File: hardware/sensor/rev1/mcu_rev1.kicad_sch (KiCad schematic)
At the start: 14 parts, among them IC1 STM8L051F3P6, J1 22-28-4044, J2 M20-9770342

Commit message: EG-49 All components reviewed, MCU and RF.
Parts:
- renumbered C3 to C2, C4 to C3, C5 to C4
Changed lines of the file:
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@@
 		(dnp no)
 		(fields_autoplaced yes)
-		(property "Reference" "C5"
+		(property "Reference" "C4"
 			(at 43.18 162.5599 0)
 			(effects
@@
 			(project "sensor_rev1"
 				(path "/d3cb7130-decc-418b-958e-e5d84a8d867f/ec220677-d66d-4ee1-961f-1c93fb46783a"
-					(reference "C5")
+					(reference "C4")
 					(unit 1)
 				)
@@
 		(dnp no)
 		(fields_autoplaced yes)
-		(property "Reference" "C3"
+		(property "Reference" "C2"
 			(at 191.77 77.4699 0)
 			(effects
@@
 			(project "sensor_rev1"
 				(path "/d3cb7130-decc-418b-958e-e5d84a8d867f/ec220677-d66d-4ee1-961f-1c93fb46783a"
-					(reference "C3")
+					(reference "C2")
 					(unit 1)
 				)
@@
 		(dnp no)
 		(fields_autoplaced yes)
-		(property "Reference" "C4"
+		(property "Reference" "C3"
 			(at 66.04 125.7299 0)
 			(effects
@@
 			(project "sensor_rev1"
 				(path "/d3cb7130-decc-418b-958e-e5d84a8d867f/ec220677-d66d-4ee1-961f-1c93fb46783a"
-					(reference "C4")
-					(unit 1)
-				)
+					(reference "C3")
+					(unit 1)
+				)

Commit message: EG-49 All  components parameters standardized for mouser.
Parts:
- C2: Manufacturer KEMET -> (none); Manufacturer Part Number C0603C102K8RACTU -> (none); Manufacturer_Name (none) -> KEMET; Manufacturer_Part_Number (none) -> C0603C102K8RACTU; Mouser Price/Stock (none) -> https://www.mouser.co.uk/en/ProductDetail/KEMET/C0603C102K8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; Supplier Link https://www.mouser.co.uk/en/ProductDetail/KEMET/C0603C102K8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 -> (none)
- C3: Manufacturer Wurth Elektronik -> (none); Manufacturer Part Number 885012206020 -> (none); Manufacturer_Name (none) -> Wurth Elektronik; Manufacturer_Part_Number (none) -> 885012206020; Mouser Price/Stock (none) -> https://pt.mouser.com/en/ProductDetail/Wurth-Elektronik/885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; Supplier Link https://pt.mouser.com/en/ProductDetail/Wurth-Elektronik/885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 -> (none)
- C4: Manufacturer YAGEO -> (none); Manufacturer Part Number CC0603KRX7R6BB103 -> (none); Manufacturer_Name (none) -> YAGEO; Manufacturer_Part_Number (none) -> CC0603KRX7R6BB103; Mouser Price/Stock (none) -> https://pt.mouser.com/en/ProductDetail/YAGEO/CC0603KRX7R6BB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; Supplier Link https://pt.mouser.com/en/ProductDetail/YAGEO/CC0603KRX7R6BB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 -> (none)
- J2: Manufacturer Harwin -> (none); Manufacturer Part Number M20-9770342 -> (none); Manufacturer_Name (none) -> Harwin; Manufacturer_Part_Number (none) -> M20-9770342; Mouser Price/Stock (none) -> https://www.mouser.co.uk/ProductDetail/Harwin/M20-9770342?q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; Supplier Link https://www.mouser.co.uk/ProductDetail/Harwin/M20-9770342?q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 -> (none)
- R1: Manufacturer Yageo -> (none); Manufacturer Part Number RC0603JR-13100RL -> (none); Manufacturer_Name (none) -> Yageo; Manufacturer_Part_Number (none) -> RC0603JR-13100RL; Mouser Price/Stock (none) -> https://pt.mouser.com/en/ProductDetail/YAGEO/RC0603JR-13100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; Supplier Link https://pt.mouser.com/en/ProductDetail/YAGEO/RC0603JR-13100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 -> (none)
- R2: Manufacturer Yageo -> (none); Manufacturer Part Number AA0603FR-072M2L -> (none); Manufacturer_Name (none) -> Yageo; Manufacturer_Part_Number (none) -> AA0603FR-072M2L; Mouser Price/Stock (none) -> https://pt.mouser.com/en/ProductDetail/YAGEO/AA0603FR-072M2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; Supplier Link https://pt.mouser.com/en/ProductDetail/YAGEO/AA0603FR-072M2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 -> (none)
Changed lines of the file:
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@@
 			)
 		)
-		(property "Supplier Link" "https://www.mouser.co.uk/ProductDetail/Harwin/M20-9770342?qs=Jph8NoUxIfVskiTzAX%252BIFA%3D%3D"
+		(property "Mouser Price/Stock" "https://www.mouser.co.uk/ProductDetail/Harwin/M20-9770342?qs=Jph8NoUxIfVskiTzAX%252BIFA%3D%3D"
 			(at 176.53 620.32 0)
 			(effects
@@
 			)
 		)
-		(property "Manufacturer" "Harwin"
+		(property "Manufacturer_Name" "Harwin"
 			(at 176.53 720.32 0)
 			(effects
@@
 			)
 		)
-		(property "Manufacturer Part Number" "M20-9770342"
+		(property "Manufacturer_Part_Number" "M20-9770342"
 			(at 176.53 820.32 0)
 			(effects
@@
 			)
 		)
-		(property "Supplier Link" "https://pt.mouser.com/en/ProductDetail/YAGEO/RC0603JR-13100RL?qs=sGAEpiMZZMvdGkrng054t8AJgcdMkx7xkQkRKZbeqEI%3D"
+		(property "Mouser Price/Stock" "https://pt.mouser.com/en/ProductDetail/YAGEO/RC0603JR-13100RL?qs=sGAEpiMZZMvdGkrng054t8AJgcdMkx7xkQkRKZbeqEI%3D"
 			(at 35.56 78.74 0)
 			(effects
@@
 			)
 		)
-		(property "Manufacturer" "Yageo"
+		(property "Manufacturer_Name" "Yageo"
 			(at 35.56 78.74 0)
 			(effects
@@
 			)
 		)
-		(property "Manufacturer Part Number" "RC0603JR-13100RL "
+		(property "Manufacturer_Part_Number" "RC0603JR-13100RL "
 			(at 35.56 78.74 0)
 			(effects
@@
 			)
 		)
-		(property "Supplier Link" "https://pt.mouser.com/en/ProductDetail/YAGEO/CC0603KRX7R6BB103?qs=sGAEpiMZZMvsSlwiRhF8qtVFUj6yLw9vFdzWWJmGTI0%3D"
+		(property "Mouser Price/Stock" "https://pt.mouser.com/en/ProductDetail/YAGEO/CC0603KRX7R6BB103?qs=sGAEpiMZZMvsSlwiRhF8qtVFUj6yLw9vFdzWWJmGTI0%3D"
 			(at 39.37 163.83 0)
 			(effects
@@
 			)
 		)
-		(property "Manufacturer" "YAGEO"
+		(property "Manufacturer_Name" "YAGEO"
 			(at 39.37 163.83 0)
 			(effects
@@
 			)
 		)
-		(property "Manufacturer Part Number" "CC0603KRX7R6BB103"
+		(property "Manufacturer_Part_Number" "CC0603KRX7R6BB103"
 			(at 39.37 163.83 0)
 			(effects
@@
 			)
 		)
-		(property "Supplier Link" "https://pt.mouser.com/en/ProductDetail/YAGEO/AA0603FR-072M2L?qs=sGAEpiMZZMvdGkrng054txzUp8gpcBx9hhxvQIhjhzKzivkvqefGPg%3D%3D"
+		(property "Mouser Price/Stock" "https://pt.mouser.com/en/ProductDetail/YAGEO/AA0603FR-072M2L?qs=sGAEpiMZZMvdGkrng054txzUp8gpcBx9hhxvQIhjhzKzivkvqefGPg%3D%3D"
 			(at 172.72 62.23 0)
 			(effects
@@
 			)
 		)
-		(property "Manufacturer" "Yageo"
+		(property "Manufacturer_Name" "Yageo"
 			(at 172.72 62.23 0)
 			(effects
@@
 			)
 		)
-		(property "Manufacturer Part Number" "AA0603FR-072M2L"
+		(property "Manufacturer_Part_Number" "AA0603FR-072M2L"
 			(at 172.72 62.23 0)
 			(effects
@@
 			)
 		)
-		(property "Supplier Link" "https://www.mouser.co.uk/en/ProductDetail/KEMET/C0603C102K8RACTU?qs=sGAEpiMZZMvsSlwiRhF8quIsB1QHp5lfG10MayaV%252Bl0%3D"
+		(property "Mouser Price/Stock" "https://www.mouser.co.uk/en/ProductDetail/KEMET/C0603C102K8RACTU?qs=sGAEpiMZZMvsSlwiRhF8quIsB1QHp5lfG10MayaV%252Bl0%3D"
 			(at 187.96 78.74 0)
 			(effects
@@
 			)
 		)
-		(property "Manufacturer" "KEMET"
+		(property "Manufacturer_Name" "KEMET"
 			(at 187.96 78.74 0)
 			(effects
@@
 			)
 		)
-		(property "Manufacturer Part Number" "C0603C102K8RACTU "
+		(property "Manufacturer_Part_Number" "C0603C102K8RACTU "
 			(at 187.96 78.74 0)
 			(effects
@@
 			)
 		)
-		(property "Supplier Link" "https://pt.mouser.com/en/ProductDetail/Wurth-Elektronik/885012206020?qs=sGAEpiMZZMvsSlwiRhF8qunkWFWGyo%252Bv87eLmDBMvaFF4rJhETyCbg%3D%3D"
+		(property "Mouser Price/Stock" "https://pt.mouser.com/en/ProductDetail/Wurth-Elektronik/885012206020?qs=sGAEpiMZZMvsSlwiRhF8qunkWFWGyo%252Bv87eLmDBMvaFF4rJhETyCbg%3D%3D"
 			(at 62.23 127 0)
 			(effects
@@
 			)
 		)
-		(property "Manufacturer" "Wurth Elektronik"
+		(property "Manufacturer_Name" "Wurth Elektronik"
 			(at 62.23 127 0)
 			(effects
@@
 			)
 		)
-		(property "Manufacturer Part Number" "885012206020"
+		(property "Manufacturer_Part_Number" "885012206020"
 			(at 62.23 127 0)
 			(effects

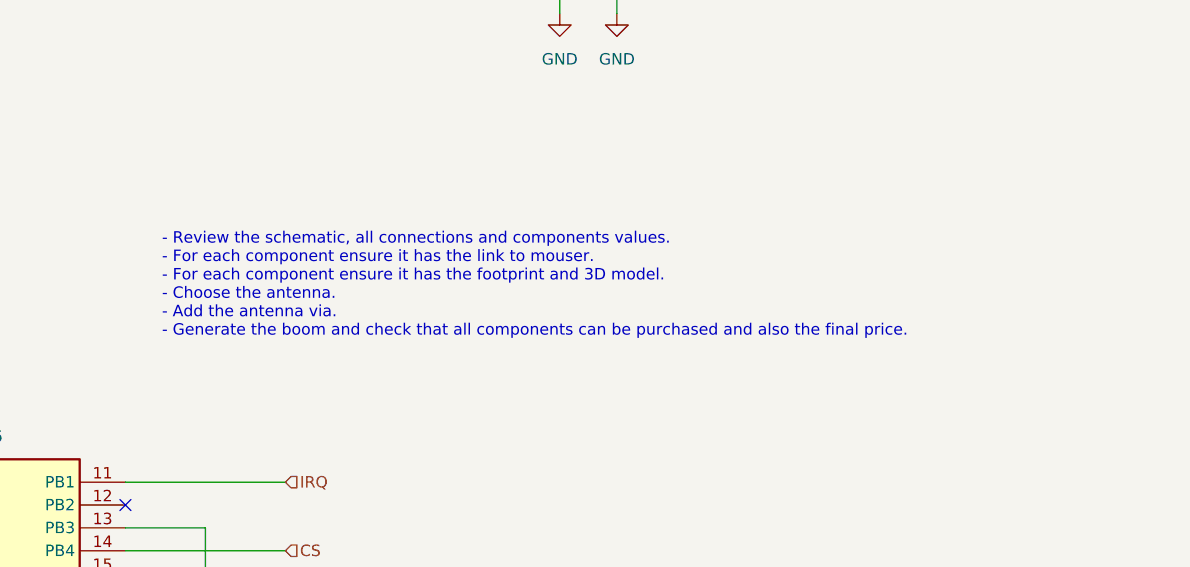
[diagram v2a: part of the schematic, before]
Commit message: EG-49 Antenna hole placed.
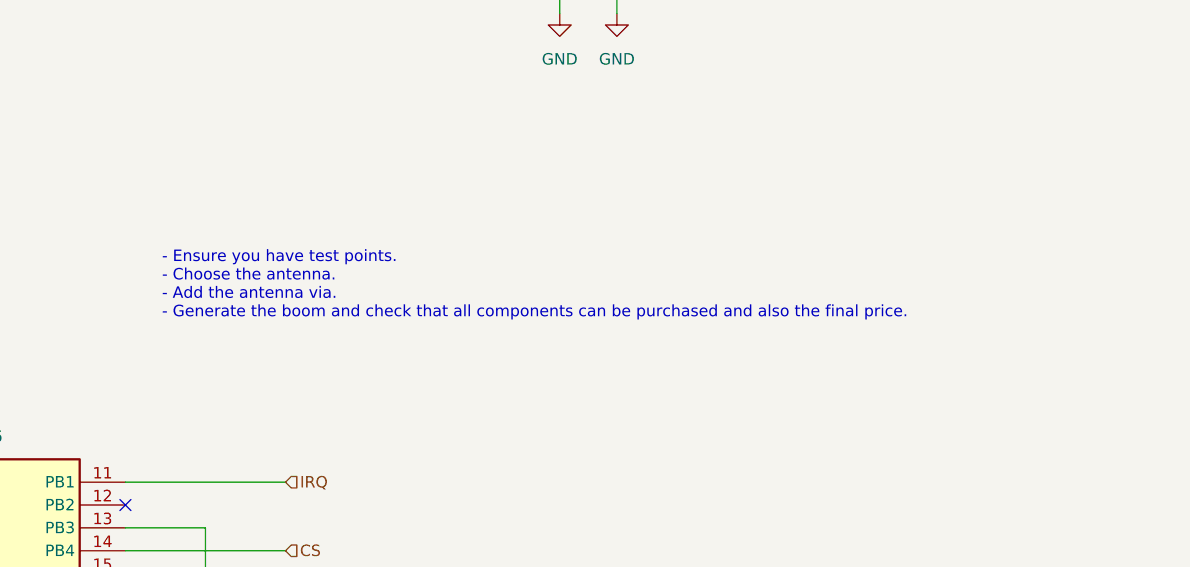
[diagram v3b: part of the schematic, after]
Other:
- note added: "- Ensure you have test points. - Choose the antenna. - Add the antenna via. - Generate the boom and check that all components can be purchased and also the final price."
- note removed: "- Review the schematic, all connections and components values. - For each component ensure it has the link to mouser. - For each component ensure it has the footprint and 3D model. - Choose the antenna. - Add the antenna via. - Generate the boom and check that all components can be purchased and also the final price."
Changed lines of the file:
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@@
 		)
 	)
-	(text "- Review the schematic, all connections and components values.\n- For each component ensure it has the link to mouser.\n- For each component ensure it has the footprint and 3D model.\n- Choose the antenna.\n- Add the antenna via.\n- Generate the boom and check that all components can be purchased and also the final price."
+	(text "- Ensure you have test points.\n- Choose the antenna.\n- Add the antenna via.\n- Generate the boom and check that all components can be purchased and also the final price."
 		(exclude_from_sim no)
 		(at 128.524 126.746 0)

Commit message: EG-49 Adjust antenna place in PCB.
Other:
- note added: "- Ensure you have test points. - Check all MCU pins once again. - Check the pull-ups enabled by SW in STM8 HAL library. - Generate the boom and check that all components can be purchased and also the final price. - Ensure ERC errros and warnings are 0."
- note removed: "- Ensure you have test points. - Choose the antenna. - Add the antenna via. - Generate the boom and check that all components can be purchased and also the final price."
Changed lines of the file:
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@@
 		)
 	)
-	(text "- Ensure you have test points.\n- Choose the antenna.\n- Add the antenna via.\n- Generate the boom and check that all components can be purchased and also the final price."
+	(text "- Ensure you have test points.\n- Check all MCU pins once again.\n- Check the pull-ups enabled by SW in STM8 HAL library.\n- Generate the boom and check that all components can be purchased and also the final price.\n- Ensure ERC errros and warnings are 0."
 		(exclude_from_sim no)
 		(at 128.524 126.746 0)

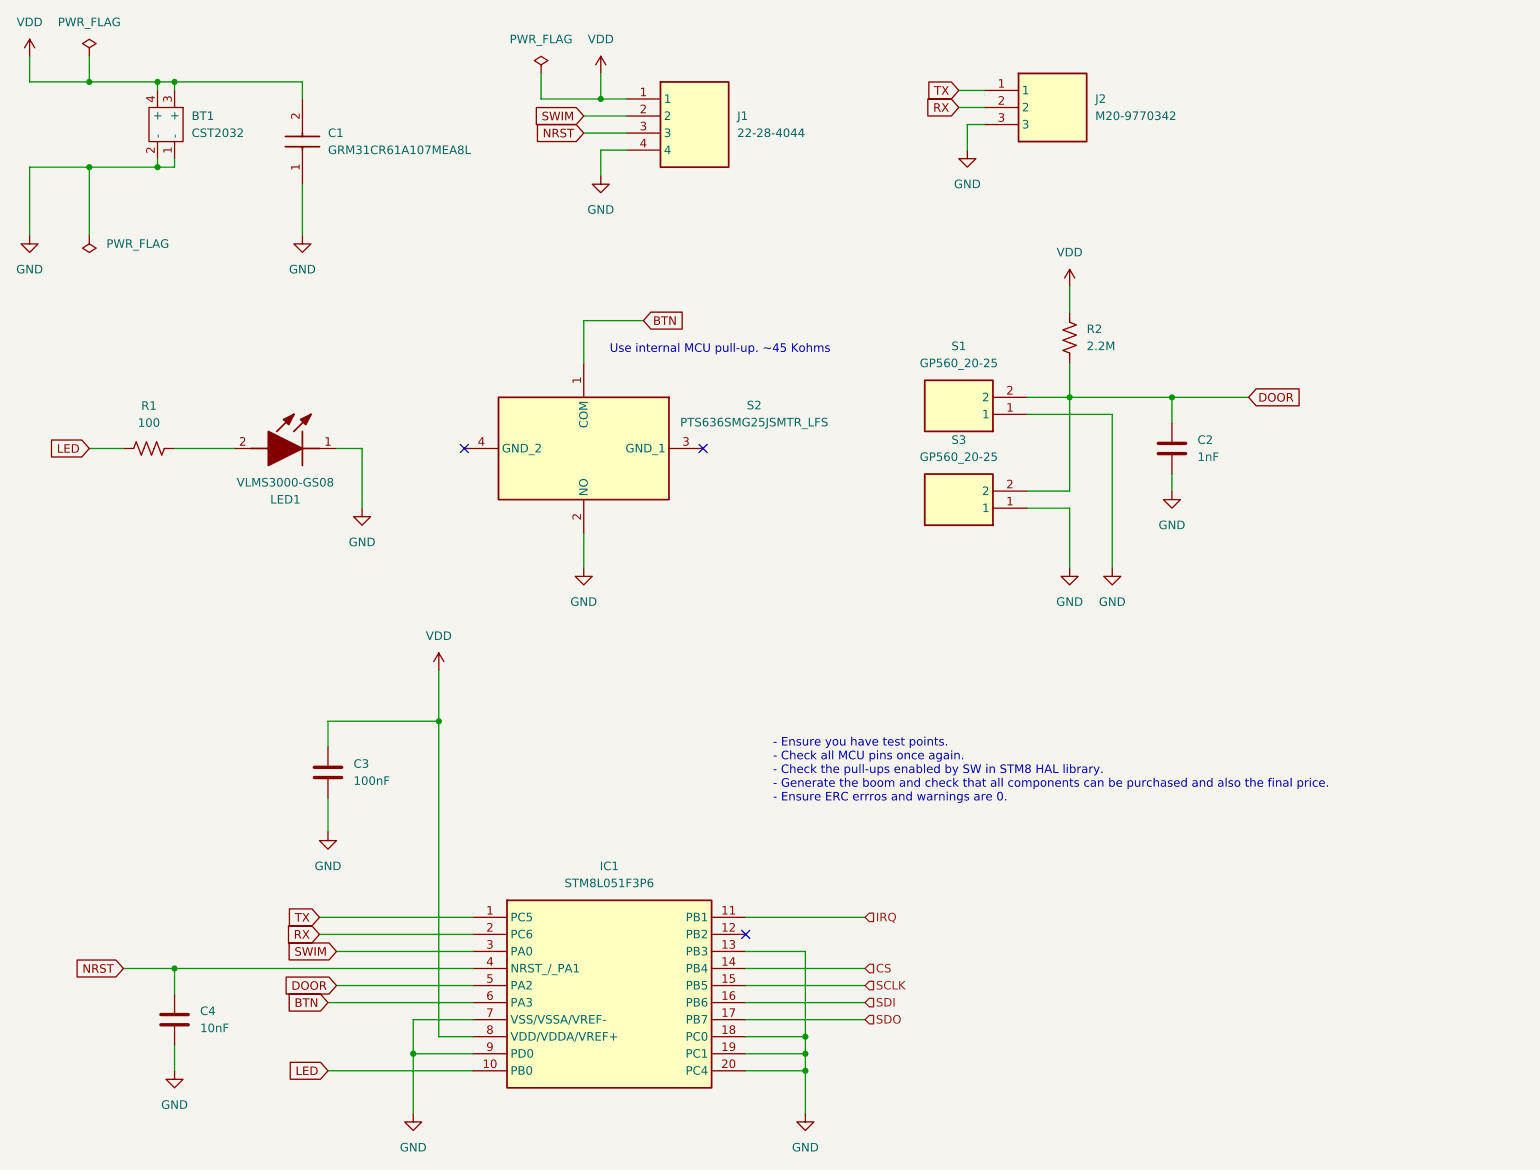
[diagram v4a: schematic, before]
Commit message: EG-49 Tests points added.
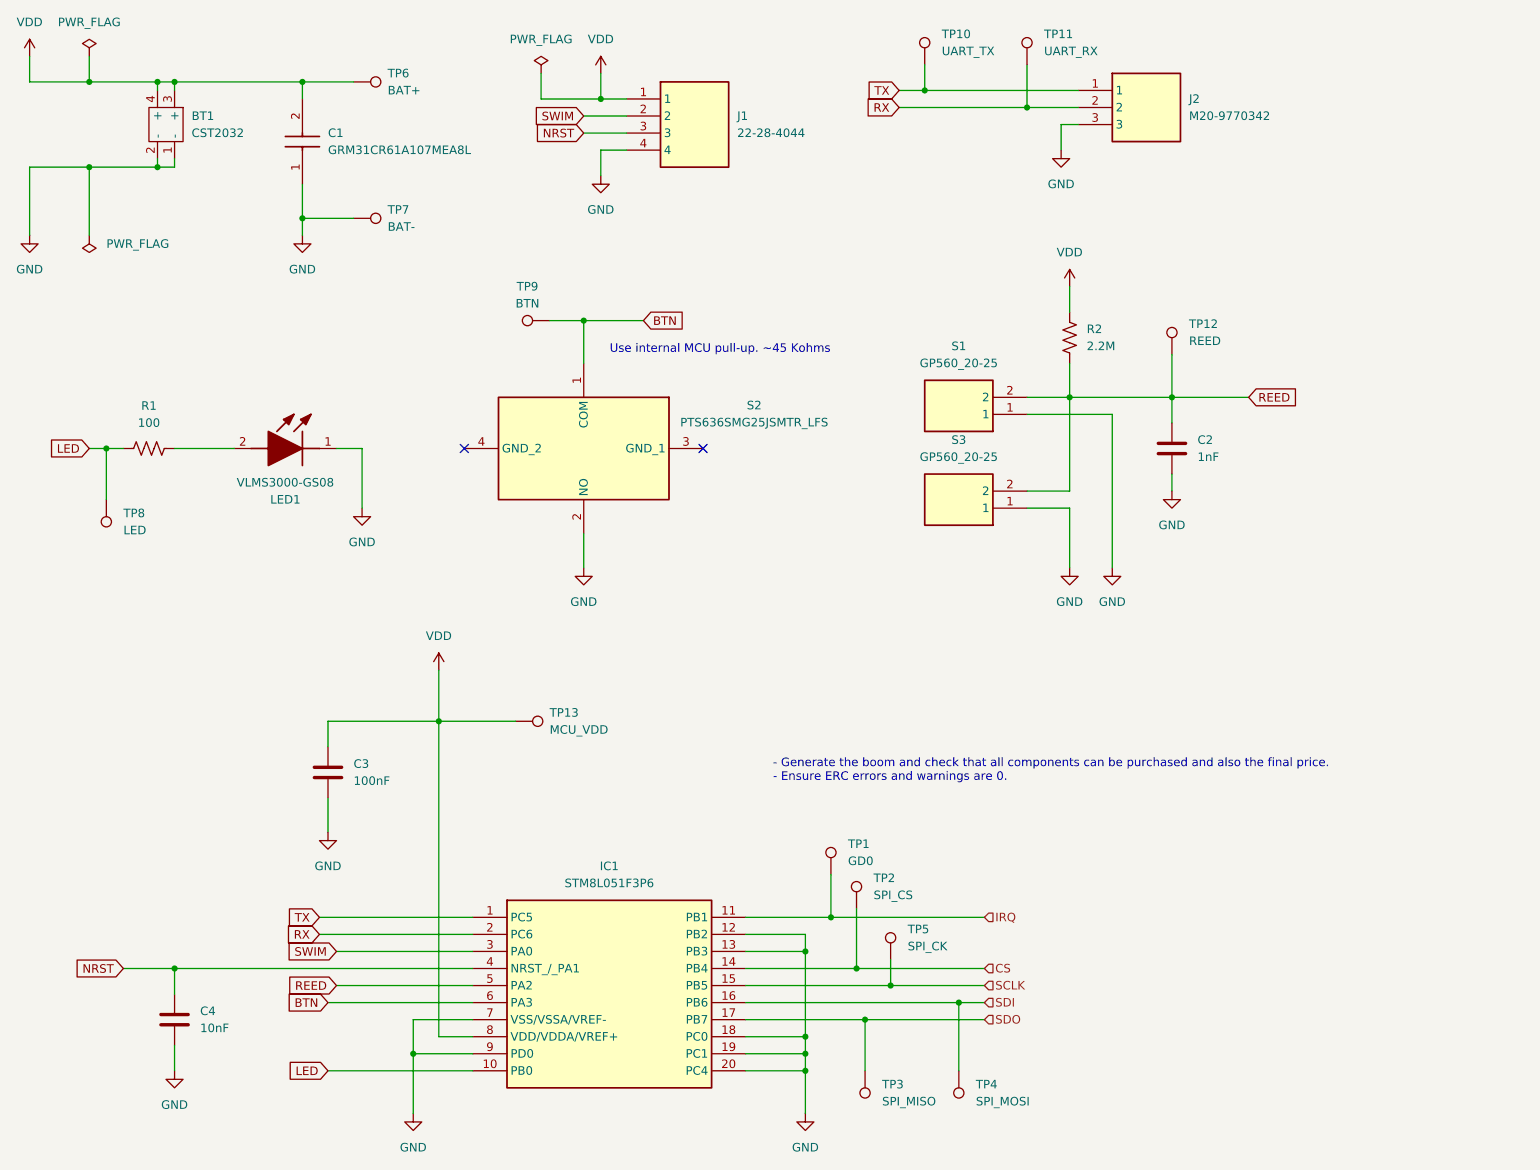
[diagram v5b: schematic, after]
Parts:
- added TP1: GD0, TestPoint:TestPoint_Pad_D1.0mm, symbol Connector:TestPoint
- added TP10: UART_TX, TestPoint:TestPoint_Pad_D1.0mm, symbol Connector:TestPoint
- added TP11: UART_RX, TestPoint:TestPoint_Pad_D1.0mm, symbol Connector:TestPoint
- added TP12: REED, TestPoint:TestPoint_Pad_D1.0mm, symbol Connector:TestPoint
- added TP13: MCU_VDD, TestPoint:TestPoint_Pad_D1.0mm, symbol Connector:TestPoint
- added TP2: SPI_CS, TestPoint:TestPoint_Pad_D1.0mm, symbol Connector:TestPoint
- added TP3: SPI_MISO, TestPoint:TestPoint_Pad_D1.0mm, symbol Connector:TestPoint
- added TP4: SPI_MOSI, TestPoint:TestPoint_Pad_D1.0mm, symbol Connector:TestPoint
- added TP5: SPI_CK, TestPoint:TestPoint_Pad_D1.0mm, symbol Connector:TestPoint
- added TP6: BAT+, TestPoint:TestPoint_Pad_D1.0mm, symbol Connector:TestPoint
- added TP7: BAT-, TestPoint:TestPoint_Pad_D1.0mm, symbol Connector:TestPoint
- added TP8: LED, TestPoint:TestPoint_Pad_D1.0mm, symbol Connector:TestPoint
- added TP9: BTN, TestPoint:TestPoint_Pad_D1.0mm, symbol Connector:TestPoint
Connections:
- net BTN: now also TP9.1
- net CS: now also TP2.1
- net GND: now also IC1.12 (PB2), TP7.1
- net IRQ: now also TP1.1
- net LED: now also TP8.1
- net RX: now also TP11.1
- net SCLK: now also TP5.1
- net SDI: now also TP4.1
- net SDO: now also TP3.1
- net TX: now also TP10.1
- net VDD: now also TP13.1, TP6.1
- net DOOR renamed REED
- net REED: now also TP12.1
- no-connect marks 3 -> 2
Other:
- note added: "- Generate the boom and check that all components can be purchased and also the final price. - Ensure ERC errors and warnings are 0."
- note removed: "- Ensure you have test points. - Check all MCU pins once again. - Check the pull-ups enabled by SW in STM8 HAL library. - Generate the boom and check that all components can be purchased and also the final price. - Ensure ERC errros and warnings are 0."
- moved on the sheet: J2
